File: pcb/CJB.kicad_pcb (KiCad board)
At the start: 2 copper layers, 106.5 x 106.5 mm, 120 parts, among them J1 USB_C_Receptacle_USB2.0_16P, J2 Micro_SD_Card, J3 Conn_01x06_Socket, J4 Conn_01x06_Socket, Q1 BUK7880, Q2 AO3400A, SW1 SW_SPDT, SW2 SW_MEC_5E, SW3 SW_MEC_5E, U1 LM1117DT-3.3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

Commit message: Change uart resistor values
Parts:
- R2, R4: value 1k -> 0
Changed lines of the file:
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@@
     (property "Sheetname" "")
     (property "Vendor" "HTL")
-    (property "VendorId" "102951")
+    (property "VendorId" "102902")
     (property "ki_description" "Resistor")
     (property "ki_keywords" "R res resistor")
@@
         (effects (font (size 1 1) (thickness 0.15)) (justify mirror))
     )
-    (fp_text value "1k" (at 0 -1.82) (layer "B.Fab")
+    (fp_text value "0" (at 0 -1.82) (layer "B.Fab")
         (effects (font (size 1 1) (thickness 0.15)) (justify mirror))
     )
@@
     (property "Sheetname" "")
     (property "Vendor" "HTL")
-    (property "VendorId" "102951")
+    (property "VendorId" "102902")
     (property "ki_description" "Resistor")
     (property "ki_keywords" "R res resistor")
@@
         (effects (font (size 1 1) (thickness 0.15)) (justify mirror))
     )
-    (fp_text value "1k" (at 0 1.778) (layer "B.Fab")
+    (fp_text value "0" (at 0 1.778) (layer "B.Fab")
         (effects (font (size 1 1) (thickness 0.15)) (justify mirror))
     )

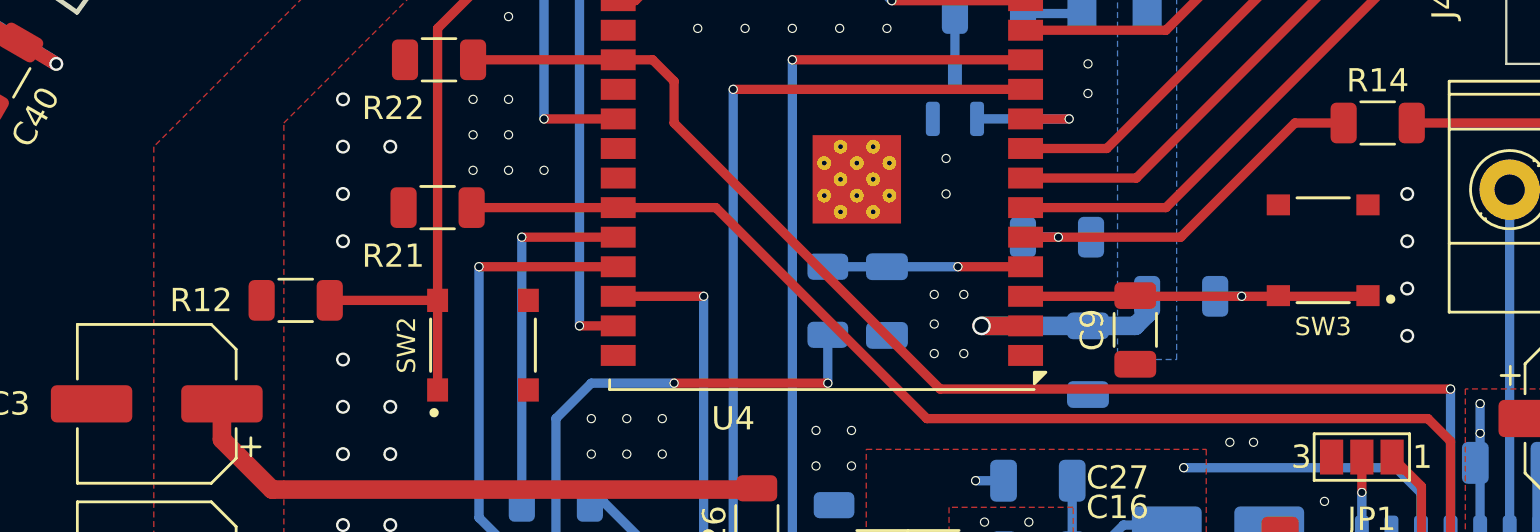
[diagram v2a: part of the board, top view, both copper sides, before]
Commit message: Add BOOT and RESET jumper
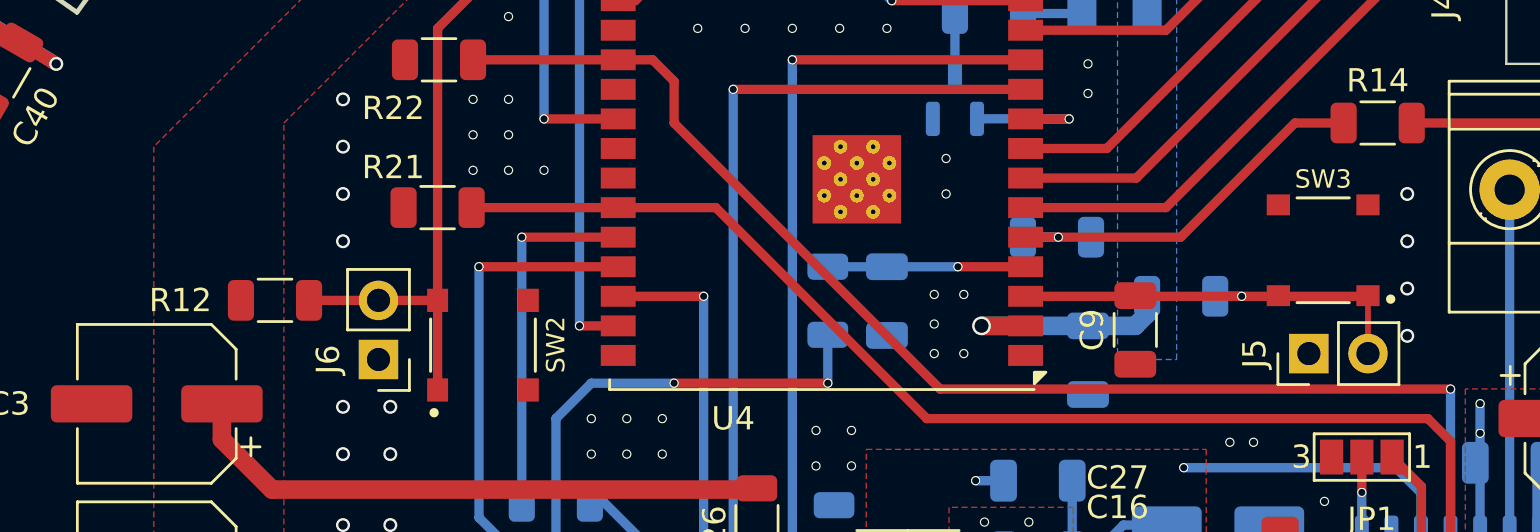
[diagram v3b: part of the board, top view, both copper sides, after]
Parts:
- added J5: Conn_01x02_Pin, Connector_PinHeader_2.54mm:PinHeader_1x02_P2.54mm_Vertical, F.Cu at (186.0, 90.6)
- added J6: Conn_01x02_Pin, Connector_PinHeader_2.54mm:PinHeader_1x02_P2.54mm_Vertical, F.Cu at (146.1, 90.8)
- moved R12 0.89 mm to (141.6, 88.3)
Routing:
- net Net-(J5-Pin_2): track 15.9 -> 18.3 mm
- net Net-(J6-Pin_2): track 28.9 -> 29.8 mm
- net GND: vias 166 -> 164

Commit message: Fix boot and power issue
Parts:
- added J7: Conn_01x02_Pin, Connector_PinHeader_2.54mm:PinHeader_1x02_P2.54mm_Vertical, F.Cu at (156.5, 67.8)
- moved R16 10.2 mm to (157.9, 70.7), turned to 180 degrees
- moved C22 1.93 mm to (188.6, 108.6), turned to 180 degrees
- moved R15 1.27 mm to (163.1, 59.9)
- moved C23 0.63 mm to (189.4, 106.7)
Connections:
- C22 pad 1: +3V3 -> +5V
- C23 pad 2: +3V3 -> +5V
- R16 pad 2: +3V3 -> Net-(J7-Pin_1)
- U5 pad 6: +3V3 -> +5V
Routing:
- net Net-(J1-SHIELD): track 33.6 -> 0.00 mm, vias 2 -> 18
- net +5V: track 459.0 -> 472.4 mm
- net +3V3: track 138.2 -> 133.9 mm, vias 20 -> 18
- net Net-(J7-Pin_1): track 0.00 -> 2.92 mm
- net /Control/SDMMC_DAT0: track 24.1 -> 22.2 mm
- net /Control/SDMMC_DAT1: track 29.7 -> 27.8 mm
- net GND: vias 164 -> 163
- added copper zone on F.Cu, net Net-(J1-SHIELD)
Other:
- board text added: "A/B"
- board text added: "BOOT"
- board text added: "D"
- board text added: "GND"
- board text added: "PROG"
- board text added: "PWR ON"
- board text added: "RESET"
- board text added: "VCC"

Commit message: Change SHDN and MUTE pins
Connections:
- R21 pad 2: ~{SHDN} -> ~{MUTE}
- R22 pad 2: ~{MUTE} -> ~{SHDN}
- U4 pad 28: ~{MUTE} -> ~{SHDN}
- U4 pad 33: ~{SHDN} -> ~{MUTE}
- U5 pad 12: ~{MUTE} -> ~{SHDN}
- U5 pad 5: ~{SHDN} -> ~{MUTE}
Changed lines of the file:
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@@
       (net 95 "unconnected-(U4-NC-Pad27)") (pinfunction "NC") (pintype "no_connect"))
     (pad "28" smd rect (at 8.75 4.445 180) (size 1.5 0.9) (layers "F.Cu" "F.Paste" "F.Mask")
-      (net 80 "~{MUTE}") (pinfunction "IO17") (pintype "bidirectional"))
+      (net 79 "~{SHDN}") (pinfunction "IO17") (pintype "bidirectional"))
     (pad "29" smd rect (at 8.75 3.175 180) (size 1.5 0.9) (layers "F.Cu" "F.Paste" "F.Mask")
       (net 96 "unconnected-(U4-IO5-Pad29)") (pinfunction "IO5") (pintype "bidirectional+no_connect"))
@@
       (net 98 "unconnected-(U4-NC-Pad32)") (pinfunction "NC") (pintype "no_connect"))
     (pad "33" smd rect (at 8.75 -1.905 180) (size 1.5 0.9) (layers "F.Cu" "F.Paste" "F.Mask")
-      (net 79 "~{SHDN}") (pinfunction "IO21") (pintype "bidirectional"))
+      (net 80 "~{MUTE}") (pinfunction "IO21") (pintype "bidirectional"))
     (pad "34" smd rect (at 8.75 -3.175 180) (size 1.5 0.9) (layers "F.Cu" "F.Paste" "F.Mask")
       (net 69 "RXD") (pinfunction "RXD0/IO3") (pintype "bidirectional"))
@@
       (net 2 "GND") (pintype "passive"))
     (pad "2" smd roundrect (at 1.4625 0) (size 1.125 1.75) (layers "F.Cu" "F.Paste" "F.Mask") (roundrect_rratio 0.2222222222)
-      (net 80 "~{MUTE}") (pintype "passive"))
+      (net 79 "~{SHDN}") (pintype "passive"))
     (model "${KICAD6_3DMODEL_DIR}/Resistor_SMD.3dshapes/R_1206_3216Metric.wrl"
       (offset (xyz 0 0 0))
@@
       (net 2 "GND") (pintype "passive"))
     (pad "2" smd roundrect (at 1.4625 0) (size 1.125 1.75) (layers "F.Cu" "F.Paste" "F.Mask") (roundrect_rratio 0.2222222222)
-      (net 79 "~{SHDN}") (pintype "passive"))
+      (net 80 "~{MUTE}") (pintype "passive"))
     (model "${KICAD6_3DMODEL_DIR}/Resistor_SMD.3dshapes/R_1206_3216Metric.wrl"
       (offset (xyz 0 0 0))
@@
       (net 1 "+5V") (pinfunction "PVDDL") (pintype "power_in"))
     (pad "5" smd roundrect (at -2.475 -0.635 90) (size 1.95 0.6) (layers "B.Cu" "B.Paste" "B.Mask") (roundrect_rratio 0.25)
-      (net 79 "~{SHDN}") (pinfunction "~{MUTE}") (pintype "input"))
+      (net 80 "~{MUTE}") (pinfunction "~{MUTE}") (pintype "input"))
     (pad "6" smd roundrect (at -2.475 -1.905 90) (size 1.95 0.6) (layers "B.Cu" "B.Paste" "B.Mask") (roundrect_rratio 0.25)
       (net 1 "+5V") (pinfunction "VDD") (pintype "power_in"))
@@
       (net 8 "GNDA") (pinfunction "GND") (pintype "power_in"))
     (pad "12" smd roundrect (at 2.475 -0.635 90) (size 1.95 0.6) (layers "B.Cu" "B.Paste" "B.Mask") (roundrect_rratio 0.25)
-      (net 80 "~{MUTE}") (pinfunction "~{SHND}") (pintype "input"))
+      (net 79 "~{SHDN}") (pinfunction "~{SHND}") (pintype "input"))
     (pad "13" smd roundrect (at 2.475 0.635 90) (size 1.95 0.6) (layers "B.Cu" "B.Paste" "B.Mask") (roundrect_rratio 0.25)
       (net 1 "+5V") (pinfunction "PVDDR") (pintype "power_in"))
@@
   (via (at 175.26 85.55) (size 0.4) (drill 0.3) (layers "F.Cu" "B.Cu") (net 78))
   (segment (start 173.736 85.55) (end 175.26 85.55) (width 0.4) (layer "B.Cu") (net 78))
-  (segment (start 192.1057 100.9592) (end 192.1057 94.3157) (width 0.4) (layer "F.Cu") (net 79))
-  (segment (start 160.5435 84.28) (end 156.35 84.28) (width 0.4) (layer "F.Cu") (net 79))
-  (segment (start 156.35 84.28) (end 150.0525 84.28) (width 0.4) (layer "F.Cu") (net 79))
-  (segment (start 192.1057 94.3157) (end 191.135 93.345) (width 0.4) (layer "F.Cu") (net 79))
-  (segment (start 191.135 93.345) (end 169.6085 93.345) (width 0.4) (layer "F.Cu") (net 79))
-  (segment (start 169.6085 93.345) (end 160.5435 84.28) (width 0.4) (layer "F.Cu") (net 79))
-  (via (at 192.1057 100.9592) (size 0.4) (drill 0.3) (layers "F.Cu" "B.Cu") (net 79))
-  (segment (start 192.1057 103.4592) (end 192.1057 100.9592) (width 0.4) (layer "B.Cu") (net 79))
-  (segment (start 157.8275 77.93) (end 156.35 77.93) (width 0.4) (layer "F.Cu") (net 80))
-  (segment (start 158.75 80.645) (end 158.75 78.8525) (width 0.4) (layer "F.Cu") (net 80))
-  (segment (start 158.75 78.8525) (end 157.8275 77.93) (width 0.4) (layer "F.Cu") (net 80))
-  (segment (start 170.18 92.075) (end 158.75 80.645) (width 0.4) (layer "F.Cu") (net 80))
-  (segment (start 192.1057 92.075) (end 170.18 92.075) (width 0.4) (layer "F.Cu") (net 80))
-  (segment (start 156.35 77.93) (end 150.114 77.93) (width 0.4) (layer "F.Cu") (net 80))
-  (via (at 192.1057 92.075) (size 0.4) (drill 0.3) (layers "F.Cu" "B.Cu") (net 80))
-  (segment (start 192.1057 92.075) (end 192.1057 98.4592) (width 0.4) (layer "B.Cu") (net 80))
+  (segment (start 157.8275 77.93) (end 156.35 77.93) (width 0.4) (layer "F.Cu") (net 79))
+  (segment (start 158.75 80.645) (end 158.75 78.8525) (width 0.4) (layer "F.Cu") (net 79))
+  (segment (start 158.75 78.8525) (end 157.8275 77.93) (width 0.4) (layer "F.Cu") (net 79))
+  (segment (start 170.18 92.075) (end 158.75 80.645) (width 0.4) (layer "F.Cu") (net 79))
+  (segment (start 192.1057 92.075) (end 170.18 92.075) (width 0.4) (layer "F.Cu") (net 79))
+  (segment (start 156.35 77.93) (end 150.114 77.93) (width 0.4) (layer "F.Cu") (net 79))
+  (via (at 192.1057 92.075) (size 0.4) (drill 0.3) (layers "F.Cu" "B.Cu") (net 79))
+  (segment (start 192.1057 92.075) (end 192.1057 98.4592) (width 0.4) (layer "B.Cu") (net 79))
+  (segment (start 192.1057 100.9592) (end 192.1057 94.3157) (width 0.4) (layer "F.Cu") (net 80))
+  (segment (start 160.5435 84.28) (end 156.35 84.28) (width 0.4) (layer "F.Cu") (net 80))
+  (segment (start 156.35 84.28) (end 150.0525 84.28) (width 0.4) (layer "F.Cu") (net 80))
+  (segment (start 192.1057 94.3157) (end 191.135 93.345) (width 0.4) (layer "F.Cu") (net 80))
+  (segment (start 191.135 93.345) (end 169.6085 93.345) (width 0.4) (layer "F.Cu") (net 80))
+  (segment (start 169.6085 93.345) (end 160.5435 84.28) (width 0.4) (layer "F.Cu") (net 80))
+  (via (at 192.1057 100.9592) (size 0.4) (drill 0.3) (layers "F.Cu" "B.Cu") (net 80))
+  (segment (start 192.1057 103.4592) (end 192.1057 100.9592) (width 0.4) (layer "B.Cu") (net 80))
   (segment (start 165.9337 99.2632) (end 162.306 99.2632) (width 0.4) (layer "F.Cu") (net 81))
   (segment (start 173.85 86.82) (end 170.942 86.82) (width 0.4) (layer "F.Cu") (net 86))

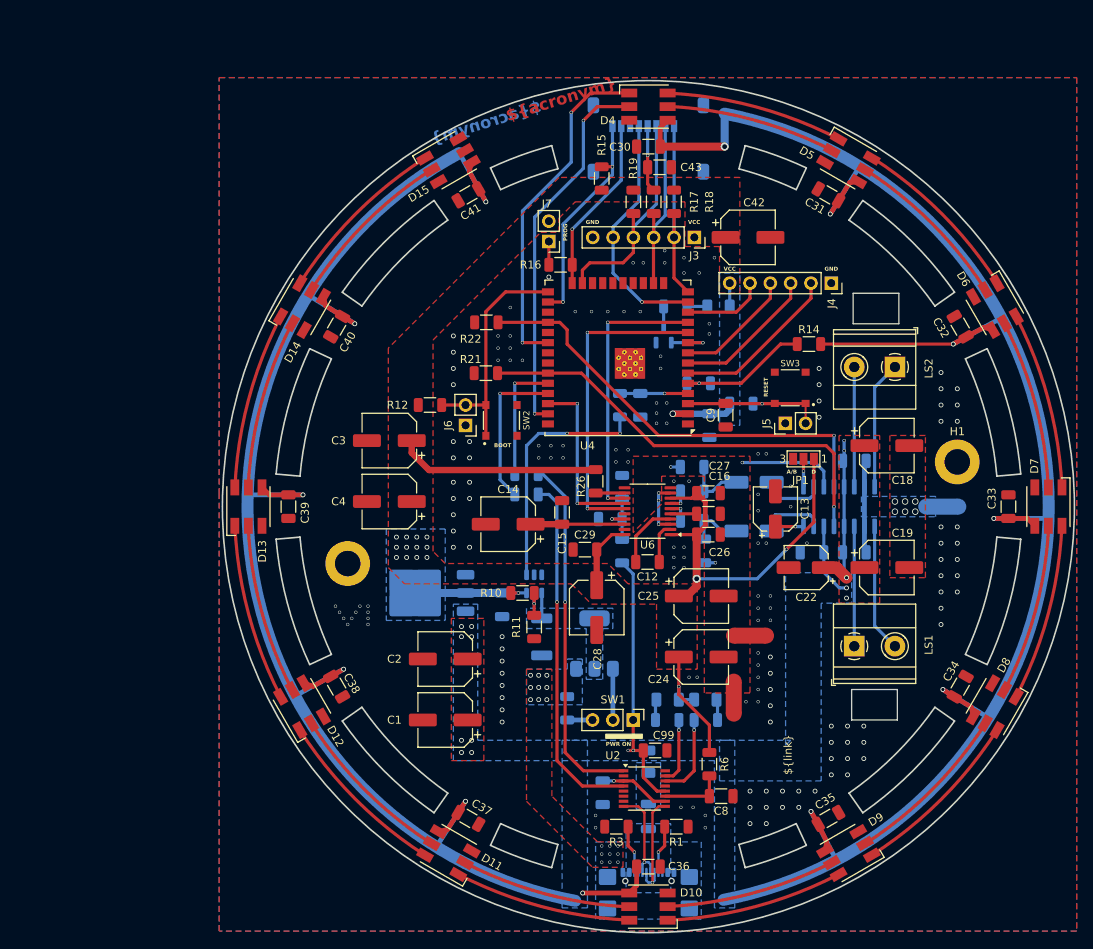
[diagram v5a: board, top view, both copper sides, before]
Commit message: Modify pcb position
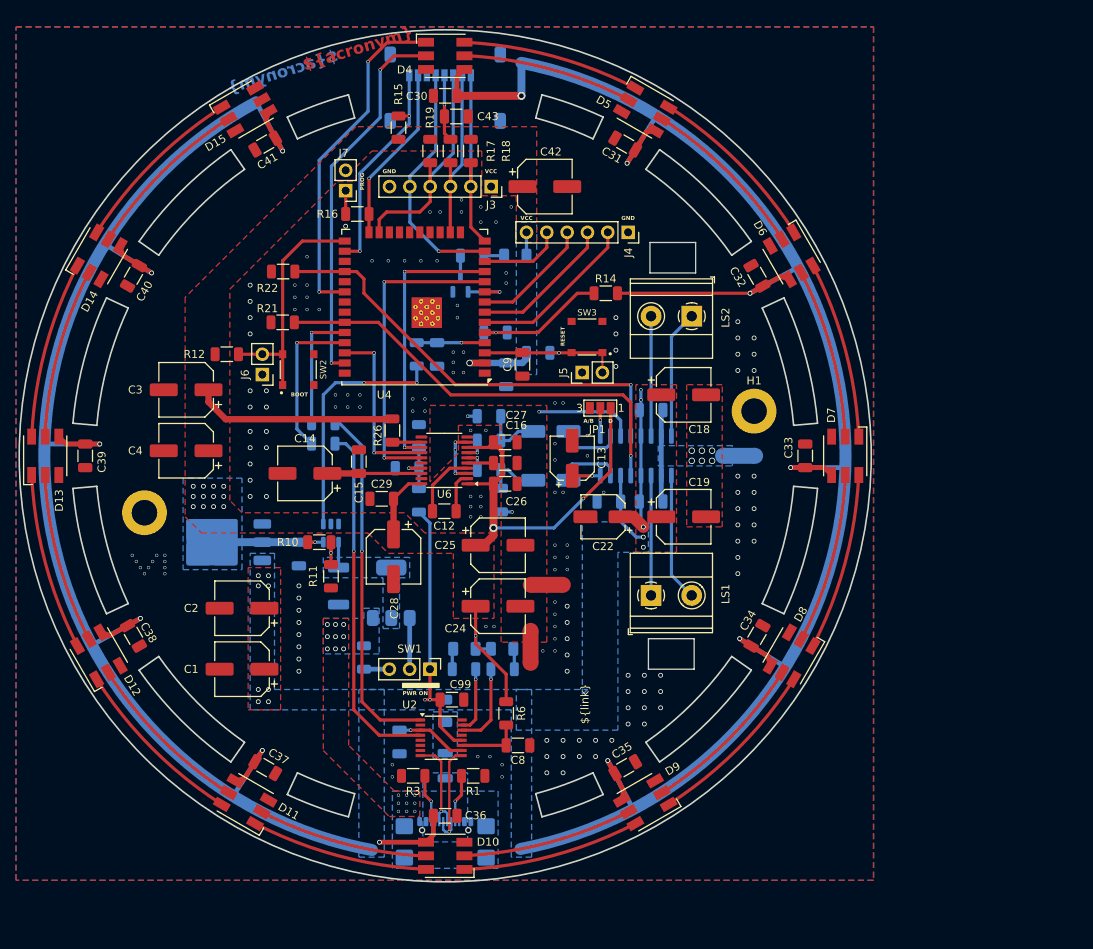
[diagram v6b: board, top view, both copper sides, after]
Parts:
- moved C5 26.2 mm to (125.2, 106.9)
- moved C10 26.2 mm to (150.5, 100.2)
- moved C13 26.2 mm to (159.4, 94.9)
- moved C16 26.2 mm to (151.0, 95.5)
- moved C18 26.2 mm to (173.3, 87.0)
- moved C20 26.2 mm to (169.2, 88.9)
- moved C23 26.2 mm to (164.0, 100.3)
- moved C25 26.2 mm to (150.1, 105.8)
- moved C28 26.2 mm to (137.0, 107.2)
- moved C30 26.2 mm to (143.5, 49.6)
- moved C31 26.2 mm to (166.0, 55.6)
- moved C32 26.2 mm to (182.5, 72.1)
- moved C33 26.2 mm to (188.5, 94.6)
- moved C34 26.2 mm to (182.5, 117.1)
- moved C41 26.2 mm to (121.0, 55.6)
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
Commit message: Optimize silkscreen text
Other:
- board text added: "Remove when Programming"
- board text removed: "PROG"
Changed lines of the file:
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@@
     (effects (font (size 1 1) (thickness 0.15)) (justify left bottom mirror))
   )
-  (gr_text "PROG" (at 132.842 60.325 90) (layer "F.SilkS")
+  (gr_text "Remove when\nProgramming" (at 127.889 60.325 90) (layer "F.SilkS")
     (effects (font (size 0.5 0.5) (thickness 0.12) bold) (justify top))
   )
